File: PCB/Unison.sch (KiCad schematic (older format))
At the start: 223 parts, among them J1 USB4085-GF-A_REVA, U2 ATmega32U4-MU, Y1 16MHz

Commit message: Update pcb.
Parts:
- removed D72, D74, D76, D78, D80, D82, D85: D, SMK_ai03_RandomKeyboardParts:D_SOD-123-Pretty, symbol Device:D
- removed EXT1, EXT2: Conn_02x05_Odd_Even, Connector_PinHeader_1.27mm:PinHeader_2x05_P1.27mm_Horizontal, symbol Connector_Generic:Conn_02x05_Odd_Even
- removed ISO-Stab1: ISO-Stabilizer, MX_Alps_Hybrid:MXOnly-ISO-StabilizerOnly-Reversed, symbol Mechanical:MountingHole
- removed JP2, JP_AUDIO1: SolderJumper_2_Open, Jumper:SolderJumper-2_P1.3mm_Open_Pad1.0x1.5mm, symbol Jumper:SolderJumper_2_Open
- removed JP_LED3, JP_LED4: SolderJumper_3_Open, Jumper:SolderJumper-3_P1.3mm_Open_Pad1.0x1.5mm_NumberLabels, symbol Jumper:SolderJumper_3_Open
- removed LED1, LED2, LED3, LED4, LED5, LED6, LED7, LED8: SK6812MINI, LED_SMD:LED_SK6812MINI_PLCC4_3.5x3.5mm_P1.75mm_TriangleMark, symbol LED:SK6812MINI
- removed LED_PAD1: Conn_01x03, SMK_hsgw:LED_WS2812_tape_10mm, symbol Connector_Generic:Conn_01x03
- removed R8, R9: 4.7k, SMK_keebio:Resistor-Hybrid, symbol Device:R
- removed SW_'1, SW_:1, SW_@1, SW_CAPS1u1, SW_E1, SW_Fn1u1, SW_H1, SW_I1, SW_ISO1, SW_O1, SW_P1, SW_Q1, SW_R1, SW_RSFT1u1, SW_T1, SW_U1, SW_W1, SW_WIN1, SW_Y1, SW_[1, SW_[3, SW_]1, SW_]2: SW_Push, MX_Alps_Hybrid:MXOnly-1U-Hotswap, symbol Switch:SW_Push
- removed SW_10, SW_ESC2, SW_[2: SW_Push, MX_Alps_Hybrid:MXOnly-1U-NoLED, symbol Switch:SW_Push
- removed SW_BS1.5u1, SW_TAB1.5u1: SW_Push, MX_Alps_Hybrid:MXOnly-1.5U-Hotswap, symbol Switch:SW_Push
- removed SW_CMD1.25u1, SW_Fn1.25u1, SW_LOPT/LALT1.25u1, SW_ROPT/KANA1.25u1: SW_Push, MX_Alps_Hybrid:MXOnly-1.25U-Hotswap, symbol Switch:SW_Push
- removed SW_ENT1.25u1: SW_Push, MX_Alps_Hybrid:MXOnly-1.25U-NoLED, symbol Switch:SW_Push
- removed SW_ENT2.25u1: SW_Push, MX_Alps_Hybrid:MXOnly-2.25U-Hotswap-ReversedStabilizers, symbol Switch:SW_Push
- removed SW_LSFT1.75u1: SW_Push, MX_Alps_Hybrid:MXOnly-1.75U-Hotswap, symbol Switch:SW_Push
- removed SW_LSPC2u1, SW_RSPC2u1: SW_Push, MX_Alps_Hybrid:MXOnly-2U-Hotswap-ReversedStabilizers, symbol Switch:SW_Push
- removed SW_RSFT1.5u1: SW_Push, MX_Alps_Hybrid:MXOnly-1.5U-NoLED, symbol Switch:SW_Push
- added D10, D100, D11, D12, D30, D41, D53, D64, D65, D77, D8, D89, D90, D91, D92, D93, D94, D95, D96, D97, D98, D99: D, SMK_ai03_RandomKeyboardParts:D_SOD-123-Pretty, symbol Device:D
- added L1, L10, L11, L12, L13, L14, L2, L3, L4, L5, L6, L7, L8, L9: YS_SK6812MINI_E_modify_GND_powerInput, symbol mx2u:YS_SK6812MINI_E_modify_GND_powerInput
- added L15: SERIAL_LED_TAPE, symbol swanmatch:SERIAL_LED_TAPE
- added OL1: OLED, symbol swanmatch:OLED
- added SW_10_2, SW_12_1, SW_12_2, SW_13_2, SW_14, SW_17_1, SW_17_2, SW_18_2, SW_19_2, SW_20_2, SW_23_2, SW_24_2, SW_25_2, SW_25_3, SW_25_4, SW_27_1, SW_27_2, SW_28_2, SW_30, SW_32_1, SW_32_2, SW_35_2, SW_37_1, SW_37_2, SW_38_2, SW_39_2, SW_40_1, SW_40_2, SW_40_3, SW_40_4, SW_42, SW_45_2, SW_45_3, SW_45_4, SW_47, SW_52, SW_57, SW_6, SW_60_1, SW_60_2, SW_62, SW_67, SW_70_2, SW_70_3, SW_72, SW_75_2, SW_7_1, SW_7_2, SW_80_2, SW_82, SW_85_2, SW_85_3, SW_85_4, SW_87, SW_8_1, SW_8_2, SW_9, SW_90, SW_91_1, SW_94, SW_95, SW_97_1, SW_97_2, SW_98_2: SW_Push, ukiha:CherryMX_MidHeight_16mm_rev2, symbol Switch:SW_Push
- added SW_RE3, SW_RE4, SW_RE5, SW_RE6: Rotary_Encoder_Switch, Rotary_Encoder:RotaryEncoder_Alps_EC11E-Switch_Vertical_H20mm, symbol Device:Rotary_Encoder_Switch
- JP_LED1: Note (none) -> Use Front LEDs
- JP_LED2: Note (none) -> Use RE2 LED
- SW_10_1: renamed from SW_CAPS1.25u1; footprint MX_Alps_Hybrid:MXOnly-1.25U-NoLED -> ukiha:CherryMX_MidHeight_16mm_rev2
- SW_13_1: renamed from SW_CTL1.25u1; footprint MX_Alps_Hybrid:MXOnly-1.5U-Hotswap -> ukiha:CherryMX_MidHeight_16mm_rev2
- SW_15: renamed from SW_LongOPT1; footprint MX_Alps_Hybrid:MXOnly-1U-Hotswap -> ukiha:CherryMX_MidHeight_16mm_rev2
- SW_16: renamed from SW_ESC1; footprint MX_Alps_Hybrid:MXOnly-1U-Hotswap -> ukiha:CherryMX_MidHeight_16mm_rev2
- SW_18_1: renamed from SW_CTL1.5u1; footprint MX_Alps_Hybrid:MXOnly-1.25U-Hotswap -> ukiha:CherryMX_MidHeight_16mm_rev2
- SW_19_1: renamed from SW_LSFT2u1; footprint MX_Alps_Hybrid:MXOnly-2U-Hotswap-ReversedStabilizers -> ukiha:CherryMX_MidHeight_16mm_rev2
- SW_20_1: renamed from SW_LongCMD1.25u1; footprint MX_Alps_Hybrid:MXOnly-1.25U-Hotswap -> ukiha:CherryMX_MidHeight_16mm_rev2
- SW_21: renamed from SW_1; footprint MX_Alps_Hybrid:MXOnly-1U-Hotswap -> ukiha:CherryMX_MidHeight_16mm_rev2
- SW_23_1: renamed from SW_S1; footprint MX_Alps_Hybrid:MXOnly-1U-Hotswap -> ukiha:CherryMX_MidHeight_16mm_rev2
- SW_24_1: renamed from SW_X1; footprint MX_Alps_Hybrid:MXOnly-1U-Hotswap -> ukiha:CherryMX_MidHeight_16mm_rev2
- SW_25_1: renamed from SW_MHEN/CMD1u1; footprint MX_Alps_Hybrid:MXOnly-1U-Hotswap -> ukiha:CherryMX_MidHeight_16mm_rev2
- SW_26: renamed from SW_2; footprint MX_Alps_Hybrid:MXOnly-1U-Hotswap -> ukiha:CherryMX_MidHeight_16mm_rev2
- SW_28_1: renamed from SW_A1; footprint MX_Alps_Hybrid:MXOnly-1U-Hotswap -> ukiha:CherryMX_MidHeight_16mm_rev2
- SW_29: renamed from SW_Z1; footprint MX_Alps_Hybrid:MXOnly-1U-Hotswap -> ukiha:CherryMX_MidHeight_16mm_rev2
- SW_31: renamed from SW_3; footprint MX_Alps_Hybrid:MXOnly-1U-Hotswap -> ukiha:CherryMX_MidHeight_16mm_rev2
- SW_34: renamed from SW_V1; footprint MX_Alps_Hybrid:MXOnly-1U-Hotswap -> ukiha:CherryMX_MidHeight_16mm_rev2
- SW_35_1: renamed from SW_LSPC2.25u1; footprint MX_Alps_Hybrid:MXOnly-2.25U-Hotswap -> ukiha:CherryMX_MidHeight_16mm_rev2
- SW_36: renamed from SW_4; footprint MX_Alps_Hybrid:MXOnly-1U-Hotswap -> ukiha:CherryMX_MidHeight_16mm_rev2
- SW_38_1: renamed from SW_D1; footprint MX_Alps_Hybrid:MXOnly-1U-Hotswap -> ukiha:CherryMX_MidHeight_16mm_rev2
- SW_39_1: renamed from SW_C1; footprint MX_Alps_Hybrid:MXOnly-1U-Hotswap -> ukiha:CherryMX_MidHeight_16mm_rev2
- SW_41: renamed from SW_5; footprint MX_Alps_Hybrid:MXOnly-1U-Hotswap -> ukiha:CherryMX_MidHeight_16mm_rev2
- SW_43: renamed from SW_F1; footprint MX_Alps_Hybrid:MXOnly-1U-Hotswap -> ukiha:CherryMX_MidHeight_16mm_rev2
- SW_45_1: renamed from SW_RSPC6.25u1; footprint MX_Alps_Hybrid:MXOnly-6.25U-Hotswap-ReversedStabilizers -> ukiha:CherryMX_MidHeight_16mm_rev2
- SW_46: renamed from SW_6; footprint MX_Alps_Hybrid:MXOnly-1U-Hotswap -> ukiha:CherryMX_MidHeight_16mm_rev2
- SW_48: renamed from SW_G1; footprint MX_Alps_Hybrid:MXOnly-1U-Hotswap -> ukiha:CherryMX_MidHeight_16mm_rev2
- SW_49: renamed from SW_B1; footprint MX_Alps_Hybrid:MXOnly-1U-Hotswap -> ukiha:CherryMX_MidHeight_16mm_rev2
- SW_50: renamed from SW_RCMD/HEN1.25u1; footprint MX_Alps_Hybrid:MXOnly-1.25U-Hotswap -> ukiha:CherryMX_MidHeight_16mm_rev2
- SW_51: renamed from SW_7; footprint MX_Alps_Hybrid:MXOnly-1U-Hotswap -> ukiha:CherryMX_MidHeight_16mm_rev2
- SW_53: renamed from SW_H2; footprint MX_Alps_Hybrid:MXOnly-1U-NoLED -> ukiha:CherryMX_MidHeight_16mm_rev2
- SW_54: renamed from SW_N1; footprint MX_Alps_Hybrid:MXOnly-1U-Hotswap -> ukiha:CherryMX_MidHeight_16mm_rev2
- SW_56: renamed from SW_8; footprint MX_Alps_Hybrid:MXOnly-1U-Hotswap -> ukiha:CherryMX_MidHeight_16mm_rev2
- SW_58: renamed from SW_J1; footprint MX_Alps_Hybrid:MXOnly-1U-Hotswap -> ukiha:CherryMX_MidHeight_16mm_rev2
- SW_59: renamed from SW_M1; footprint MX_Alps_Hybrid:MXOnly-1U-Hotswap -> ukiha:CherryMX_MidHeight_16mm_rev2
- SW_61: renamed from SW_9; footprint MX_Alps_Hybrid:MXOnly-1U-Hotswap -> ukiha:CherryMX_MidHeight_16mm_rev2
- SW_63: renamed from SW_K1; footprint MX_Alps_Hybrid:MXOnly-1U-Hotswap -> ukiha:CherryMX_MidHeight_16mm_rev2
- SW_64: renamed from SW_<1; footprint MX_Alps_Hybrid:MXOnly-1U-Hotswap -> ukiha:CherryMX_MidHeight_16mm_rev2
- SW_65: renamed from SW_ROPT/KANA1.25u2; footprint MX_Alps_Hybrid:MXOnly-1.25U-Hotswap -> ukiha:CherryMX_MidHeight_16mm_rev2
- SW_68: renamed from SW_L1; footprint MX_Alps_Hybrid:MXOnly-1U-Hotswap -> ukiha:CherryMX_MidHeight_16mm_rev2
- SW_69: renamed from SW_>1; footprint MX_Alps_Hybrid:MXOnly-1U-Hotswap -> ukiha:CherryMX_MidHeight_16mm_rev2
- SW_70_1: renamed from SW_LEFT1; footprint MX_Alps_Hybrid:MXOnly-1U-Hotswap -> ukiha:CherryMX_MidHeight_16mm_rev2
- SW_71: renamed from SW_-1; footprint MX_Alps_Hybrid:MXOnly-1U-Hotswap -> ukiha:CherryMX_MidHeight_16mm_rev2
- SW_73: renamed from SW_;1; footprint MX_Alps_Hybrid:MXOnly-1U-Hotswap -> ukiha:CherryMX_MidHeight_16mm_rev2
- SW_74: renamed from SW_/1; footprint MX_Alps_Hybrid:MXOnly-1U-Hotswap -> ukiha:CherryMX_MidHeight_16mm_rev2
- SW_75_1: renamed from SW_MENU/ROPT1; footprint MX_Alps_Hybrid:MXOnly-1U-Hotswap -> ukiha:CherryMX_MidHeight_16mm_rev2
- SW_76: renamed from SW_0; footprint MX_Alps_Hybrid:MXOnly-1U-Hotswap -> ukiha:CherryMX_MidHeight_16mm_rev2
- SW_78: renamed from SW_ENT1.5u1; footprint MX_Alps_Hybrid:MXOnly-1.5U-NoLED -> ukiha:CherryMX_MidHeight_16mm_rev2
- SW_79: renamed from SW_RSFT1.75u1; footprint MX_Alps_Hybrid:MXOnly-1.75U-Hotswap -> ukiha:CherryMX_MidHeight_16mm_rev2
- SW_80_1: renamed from SW_RIGHT1; footprint MX_Alps_Hybrid:MXOnly-1U-Hotswap -> ukiha:CherryMX_MidHeight_16mm_rev2
- SW_81: renamed from SW_\1; footprint MX_Alps_Hybrid:MXOnly-1U-Hotswap -> ukiha:CherryMX_MidHeight_16mm_rev2
- SW_83: renamed from SW_'2; footprint MX_Alps_Hybrid:MXOnly-1U-NoLED -> ukiha:CherryMX_MidHeight_16mm_rev2
- SW_84: renamed from SW_up1; footprint MX_Alps_Hybrid:MXOnly-1U-Hotswap -> ukiha:CherryMX_MidHeight_16mm_rev2
- SW_85_1: renamed from SW_DOWN1; footprint MX_Alps_Hybrid:MXOnly-1U-Hotswap -> ukiha:CherryMX_MidHeight_16mm_rev2
- SW_86: renamed from SW_=1; footprint MX_Alps_Hybrid:MXOnly-1U-Hotswap -> ukiha:CherryMX_MidHeight_16mm_rev2
- SW_89: renamed from SW_Fn1.5u1; footprint MX_Alps_Hybrid:MXOnly-1.5U-NoLED -> ukiha:CherryMX_MidHeight_16mm_rev2
- SW_96: renamed from SW_`1; footprint MX_Alps_Hybrid:MXOnly-1U-Hotswap -> ukiha:CherryMX_MidHeight_16mm_rev2
- SW_98_1: renamed from SW_FN1.75u1; footprint MX_Alps_Hybrid:MXOnly-1.75U-NoLED -> ukiha:CherryMX_MidHeight_16mm_rev2
- renumbered D66 to D1, D71 to D102, D67 to D13, D73 to D14, D11 to D15, D7 to D16, D8 to D17, D9 to D18, D10 to D19, D86 to D2, D16 to D20, D12 to D21, D13 to D22, D14 to D23, D15 to D24, D75 to D25, D21 to D26, D17 to D27, D18 to D28, D19 to D29, D1 to D3, D25 to D31, D22 to D32, D23 to D33, D24 to D34, D20 to D35, D77 to D36, D29 to D37, D26 to D38, D27 to D39, D2 to D4, D28 to D40, D33 to D42, D38 to D43, D39 to D44, D40 to D45, D68 to D46, D79 to D47, D37 to D48, D42 to D49, D3 to D5, D43 to D50, D44 to D51, D69 to D52, D41 to D54, D47 to D55, D48 to D56, D49 to D57, D45 to D58, D81 to D59, D4 to D6, D46 to D60, D30 to D61, D31 to D62, D32 to D63, D51 to D66, D34 to D67, D35 to D68, D36 to D69, D5 to D7, D50 to D70, D84 to D71, D56 to D72, D52 to D73, D53 to D74, D54 to D75, D55 to D76, D61 to D78, D57 to D79, D58 to D80, D59 to D81, D60 to D82, D62 to D84, D63 to D85, D64 to D86, D70 to D87, D65 to D88, D6 to D9, R7 to R1, R5 to R4, R1 to R5, R2 to R6, R4 to R7, R3 to R8, R6 to R9, U2 to U1
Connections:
- net labels added: AUDIO1, AUDIO2[Reserve], RE3_1, RE3_2, RE3_A, RE3_B, RE4_1, RE4_2, RE4_A, RE4_B, RE5_1, RE5_2, RE5_A, RE5_B, RE6_1, RE6_2, RE6_A, RE6_B, SCL_RE2B, SDA_RE2A
- net labels removed: AUDIO, RE2_A, RE2_B, Reserve_PB4, Reserve_PB5, Reserve_PB6, Reserve_PC6, Reserve_PD2-RX, Reserve_PD3-TX, SCL, SDA, pin11
- wire segments 323 -> 585
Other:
- note added: "Audio pins\nGroup1: B5, B6, B7\nGroup2: C4, C5, C6"
- note added: "Layer Indicator"
- note added: "Optional: OLED alternate"
- note added: "Rotary Encoder Indicator (2nd R.E. is OLED alternate)"
- note added: "SW_01"
- note added: "SW_02"
- note added: "SW_03"
- note added: "SW_04"
- note added: "SW_05"
- note added: "SW_92"
- note added: "SW_93\nReserved"
- note added: "Volume Indicator"
- note removed: "Use Left LEDs"
- note removed: "Use Right LEDs"
- moved on the sheet: C1, C2, C3, C4, C5, C6, C7, D1, D102, D13, D14, D15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

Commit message: Update v01完成
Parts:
- removed L15: SERIAL_LED_TAPE, symbol swanmatch:SERIAL_LED_TAPE
- added J2: Conn_02x01, Connector_PinHeader_2.54mm:PinHeader_2x01_P2.54mm_Vertical, symbol Connector_Generic:Conn_02x01
- added L15: SERIAL_LED_TAPE, ukiha:StripLED_rev3, symbol local_library:SERIAL_LED_TAPE
- added SW_23_3, SW_32_3: SW_Push, ukiha:CherryMX_MidHeight_16mm_rev2, symbol Switch:SW_Push
- C1, C2, C3, C4, C5, C6, C7: footprint Capacitor_SMD:C_0805_2012Metric_Pad1.15x1.40mm_HandSolder -> Capacitor_SMD:C_0805_2012Metric_Pad1.18x1.45mm_HandSolder
- D1, D10, D100, D11, D12, D13, D14, D15, D16, D17, D18, D19, D2, D20, D21, D22, D23, D24, D25, D26, D27, D28, D29, D3, D30, D31, D32, D33, D34, D35, D36, D37, D38, D39, D4, D40, D41, D42, D43, D44, D45, D46, D47, D48, D49, D5, D50, D51, D52, D53, D54, D55, D56, D57, D58, D59, D6, D60, D61, D62, D63, D64, D65, D66, D67, D68, D69, D7, D70, D71, D72, D73, D74, D75, D76, D77, D78, D79, D8, D80, D81, D82, D83, D84, D85, D86, D87, D88, D89, D9, D90, D91, D92, D93, D94, D95, D96, D97, D98, D99: footprint SMK_ai03_RandomKeyboardParts:D_SOD-123-Pretty -> Diode_SMD:D_SOD-123
- J1: footprint Connector_USB:USB_C_Receptacle_GCT_USB4085_pad_modified -> USB4085:GCT_USB4085-GF-A_REVA
- L1, L10, L11, L12, L13, L14, L2, L3, L4, L5, L6, L7, L8, L9: footprint (none) -> mx2u:YS-SK6812MINI-E
- OL1: footprint (none) -> ukiha:OLED_rev2
- R1, R4, R5, R6, R7, R8, R9: footprint Resistor_SMD:R_0805_2012Metric_Pad1.15x1.40mm_HandSolder -> Resistor_SMD:R_0805_2012Metric_Pad1.20x1.40mm_HandSolder
- ResetSW1: footprint SMK_ai03_RandomKeyboardParts:SKQG-1155865 -> Button_Switch_SMD:SW_SPST_SKQG_WithStem
- SW_10_2, SW_19_2, SW_24_2, SW_39_2, SW_45_4: footprint ukiha:CherryMX_MidHeight_16mm_rev2 -> ukiha:CherryMX_MidHeight_16mm_rev2_2u_guide
- SW_17_2, SW_18_2, SW_23_2, SW_25_3, SW_32_2, SW_37_2, SW_38_2, SW_40_2, SW_45_2, SW_70_2, SW_75_2, SW_7_2, SW_85_3, SW_8_2, SW_97_2, SW_98_2: footprint ukiha:CherryMX_MidHeight_16mm_rev2 -> ukiha:CherryMX_MidHeight_16mm_rev2_1.5u_guide
- SW_20_2, SW_25_4, SW_35_2, SW_40_3, SW_40_4, SW_45_3, SW_70_3, SW_80_2, SW_85_2, SW_85_4: footprint ukiha:CherryMX_MidHeight_16mm_rev2 -> ukiha:CherryMX_MidHeight_16mm_rev2_1.25u_guide
- SW_25_2, SW_60_2: footprint ukiha:CherryMX_MidHeight_16mm_rev2 -> ukiha:CherryMX_MidHeight_16mm_rev2_2U_vertical_guide
- U1: footprint SMK_keebio:QFN-44-1EP_7x7mm_Pitch0.5mm -> swanmatch:QFN-44-1EP_7x7mm_Pitch0.5mm
- renumbered SW_91_1 to SW_91
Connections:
- wire segments 585 -> 587
- no-connect marks 4 -> 6
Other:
- note added: "1 2 3 4 5 6 7 8 9 10 11 12 13 14 15 16 17\n17 16 15 14 13 12 11 10 9 8 7 6 5 4 3 2 1"
- note added: "1 2 3 4 5 6 7 8 9/0"
- note added: "SW_93\nReserve"
- note removed: "SW_93\nReserved"
- moved on the sheet: D8, JP_LED1, JP_LED2, L1, L10, L11, L12, L13, L14, L2, L3, L4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

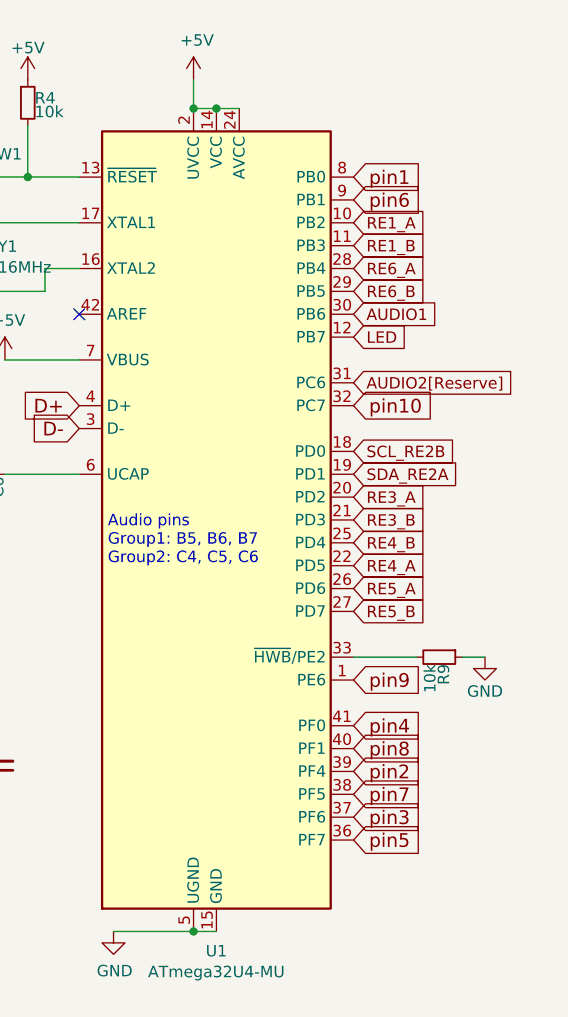
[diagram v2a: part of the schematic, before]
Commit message: Update: Change MCU from ATMega32u4-MU  to ATMega32u4-AU.
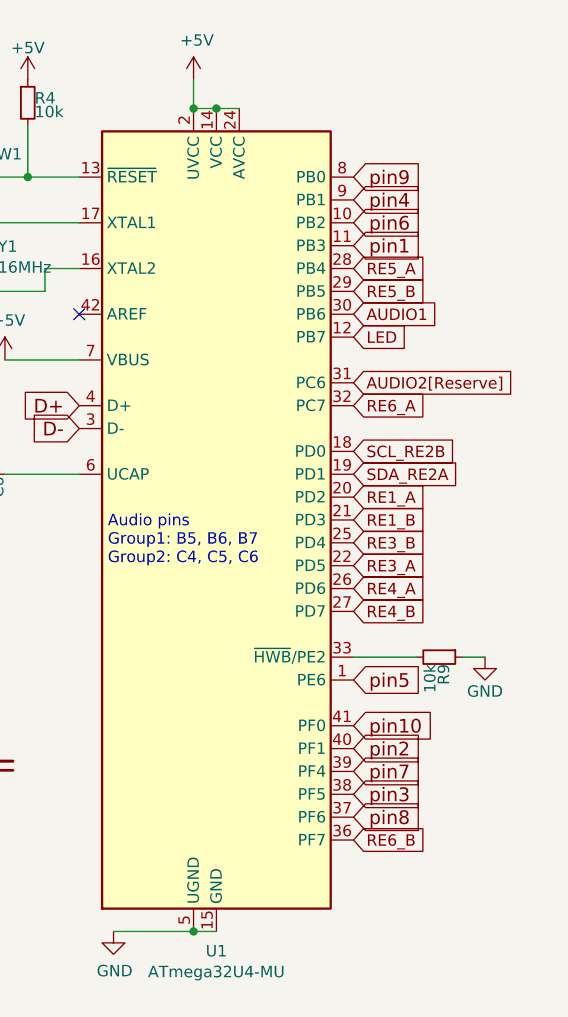
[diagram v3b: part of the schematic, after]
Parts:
- U1: footprint swanmatch:QFN-44-1EP_7x7mm_Pitch0.5mm -> keebio:ATMEGA32U4-AU
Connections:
- net RE1_A: now also U1.20 (PD2); no longer U1.10 (PB2)
- net RE1_B: now also U1.21 (PD3); no longer U1.11 (PB3)
- net RE3_A: now also U1.22 (PD5); no longer U1.20 (PD2)
- net RE3_B: now also U1.25 (PD4); no longer U1.21 (PD3)
- net RE4_A: now also U1.26 (PD6); no longer U1.22 (PD5)
- net RE4_B: now also U1.27 (PD7); no longer U1.25 (PD4)
- net RE5_A: now also U1.28 (PB4); no longer U1.26 (PD6)
- net RE5_B: now also U1.29 (PB5); no longer U1.27 (PD7)
- net RE6_A: now also U1.32 (PC7); no longer U1.28 (PB4)
- net RE6_B: now also U1.36 (PF7); no longer U1.29 (PB5)
- net pin1: now also U1.11 (PB3); no longer U1.8 (PB0)
- net pin10: now also U1.41 (PF0); no longer U1.32 (PC7)
- net pin2: now also U1.40 (PF1); no longer U1.39 (PF4)
- net pin3: now also U1.38 (PF5); no longer U1.37 (PF6)
- net pin4: now also U1.9 (PB1); no longer U1.41 (PF0)
- net pin5: now also U1.1 (PE6); no longer U1.36 (PF7)
- net pin6: now also U1.10 (PB2); no longer U1.9 (PB1)
- net pin7: now also U1.39 (PF4); no longer U1.38 (PF5)
- net pin8: now also U1.37 (PF6); no longer U1.40 (PF1)
- net pin9: now also U1.8 (PB0); no longer U1.1 (PE6)
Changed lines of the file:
@@
 	-1   0    0    1
 $EndComp
-Text GLabel 15300 2225 2    60   Input ~ 0
+Text GLabel 15300 2325 2    60   Input ~ 0
 pin6
-Text GLabel 15300 5025 2    60   Input ~ 0
+Text GLabel 15300 4325 2    60   Input ~ 0
 pin5
-Text GLabel 15300 4525 2    60   Input ~ 0
+Text GLabel 15300 2225 2    60   Input ~ 0
 pin4
-Text GLabel 15300 4925 2    60   Input ~ 0
+Text GLabel 15300 4825 2    60   Input ~ 0
 pin3
-Text GLabel 15300 4725 2    60   Input ~ 0
+Text GLabel 15300 4625 2    60   Input ~ 0
 pin2
-Text GLabel 15300 2125 2    60   Input ~ 0
+Text GLabel 15300 2425 2    60   Input ~ 0
 pin1
-Text GLabel 15300 3125 2    60   Input ~ 0
+Text GLabel 15300 4525 2    60   Input ~ 0
 pin10
 Wire Wire Line
@@
 F 0 "U1" H 14700 1739 50  0000 C CNN
 F 1 "ATmega32U4-MU" H 14700 1648 50  0000 C CNN
-F 2 "swanmatch:QFN-44-1EP_7x7mm_Pitch0.5mm" H 14700 3625 50  0001 C CIN
+F 2 "keebio:ATMEGA32U4-AU" H 14700 3625 50  0001 C CIN
 F 3 "http://ww1.microchip.com/downloads/en/DeviceDoc/Atmel-7766-8-bit-AVR-ATmega16U4-32U4_Datasheet.pdf" H 14700 3625 50  0001 C CNN
 F 4 "C45874" H 14700 3625 50  0001 C CNN "LCSC"
@@
 	1    0    0    -1
 $EndComp
-Text GLabel 15300 2325 2    50   Input ~ 0
+Text GLabel 15300 3525 2    50   Input ~ 0
 RE1_A
-Text GLabel 15300 2425 2    50   Input ~ 0
+Text GLabel 15300 3625 2    50   Input ~ 0
 RE1_B
 $Comp
@@
 Wire Wire Line
 	925  10025 925  10225
-Text GLabel 15300 2525 2    50   Input ~ 0
+Text GLabel 15300 3125 2    50   Input ~ 0
 RE6_A
 Text GLabel 15300 2725 2    50   Input ~ 0
@@
 Text GLabel 15300 2825 2    50   Input ~ 0
 LED
-Text GLabel 15300 2625 2    50   Input ~ 0
+Text GLabel 15300 5025 2    50   Input ~ 0
 RE6_B
-Text GLabel 15300 4325 2    60   Input ~ 0
+Text GLabel 15300 2125 2    60   Input ~ 0
 pin9
-Text GLabel 15300 4625 2    60   Input ~ 0
+Text GLabel 15300 4925 2    60   Input ~ 0
 pin8
-Text GLabel 15300 4825 2    60   Input ~ 0
+Text GLabel 15300 4725 2    60   Input ~ 0
 pin7
 $Comp
@@
 Text Notes 14225 3825 0    50   ~ 0
 Audio pins\nGroup1: B5, B6, B7\nGroup2: C4, C5, C6
-Text GLabel 15300 3525 2    50   Input ~ 0
+Text GLabel 15300 3825 2    50   Input ~ 0
 RE3_A
-Text GLabel 15300 3625 2    50   Input ~ 0
+Text GLabel 15300 3725 2    50   Input ~ 0
 RE3_B
-Text GLabel 15300 3825 2    50   Input ~ 0
+Text GLabel 15300 3925 2    50   Input ~ 0
 RE4_A
-Text GLabel 15300 3725 2    50   Input ~ 0
+Text GLabel 15300 4025 2    50   Input ~ 0
 RE4_B
-Text GLabel 15300 3925 2    50   Input ~ 0
+Text GLabel 15300 2525 2    50   Input ~ 0
 RE5_A
-Text GLabel 15300 4025 2    50   Input ~ 0
+Text GLabel 15300 2625 2    50   Input ~ 0
 RE5_B
 Text GLabel 4450 11000 2    50   Input ~ 0

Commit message: Update: MCUをMUからAUに変更し、配線をやり直した。
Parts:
- SW_37_2: footprint ukiha:CherryMX_MidHeight_16mm_rev2_1.5u_guide -> ukiha:CherryMX_MidHeight_16mm_rev2_1.5u_alt_guide
- U1: value ATmega32U4-MU -> ATmega32U4-AU; symbol MCU_Microchip_ATmega:ATmega32U4-MU -> MCU_Microchip_ATmega:ATmega32U4-AU
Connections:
- net GND: no longer U1.45 (GND)
- net RE1_A: now also U1.8 (PB0); no longer U1.20 (PD2)
- net RE1_B: now also U1.9 (PB1); no longer U1.21 (PD3)
- net RE3_A: now also U1.21 (PD3); no longer U1.22 (PD5)
- net RE3_B: now also U1.20 (PD2); no longer U1.25 (PD4)
- net RE4_A: now also U1.22 (PD5); no longer U1.26 (PD6)
- net RE4_B: now also U1.25 (PD4); no longer U1.27 (PD7)
- net RE5_A: now also U1.26 (PD6); no longer U1.28 (PB4)
- net RE5_B: now also U1.27 (PD7); no longer U1.29 (PB5)
- net RE6_A: now also U1.28 (PB4); no longer U1.32 (PC7)
- net RE6_B: now also U1.29 (PB5); no longer U1.36 (PF7)
- net pin10: now also U1.32 (PC7); no longer U1.41 (PF0)
- net pin2: now also U1.1 (PE6); no longer U1.40 (PF1)
- net pin3: now also U1.40 (PF1); no longer U1.38 (PF5)
- net pin4: now also U1.38 (PF5); no longer U1.9 (PB1)
- net pin5: now also U1.36 (PF7); no longer U1.1 (PE6)
- net pin7: now also U1.41 (PF0); no longer U1.39 (PF4)
- net pin8: now also U1.39 (PF4); no longer U1.37 (PF6)
- net pin9: now also U1.37 (PF6); no longer U1.8 (PB0)
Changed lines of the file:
@@
 Text GLabel 15300 2325 2    60   Input ~ 0
 pin6
-Text GLabel 15300 4325 2    60   Input ~ 0
+Text GLabel 15300 5025 2    60   Input ~ 0
 pin5
-Text GLabel 15300 2225 2    60   Input ~ 0
-pin4
 Text GLabel 15300 4825 2    60   Input ~ 0
-pin3
+pin4
 Text GLabel 15300 4625 2    60   Input ~ 0
+pin3
+Text GLabel 15300 4325 2    60   Input ~ 0
 pin2
 Text GLabel 15300 2425 2    60   Input ~ 0
 pin1
-Text GLabel 15300 4525 2    60   Input ~ 0
+Text GLabel 15300 3125 2    60   Input ~ 0
 pin10
 Wire Wire Line
@@
 	13250 4900 13500 4900
 $Comp
-L MCU_Microchip_ATmega:ATmega32U4-MU U1
+L MCU_Microchip_ATmega:ATmega32U4-AU U1
 U 1 1 5D93C3AA
 P 14700 3625
 F 0 "U1" H 14700 1739 50  0000 C CNN
-F 1 "ATmega32U4-MU" H 14700 1648 50  0000 C CNN
+F 1 "ATmega32U4-AU" H 14700 1648 50  0000 C CNN
 F 2 "keebio:ATMEGA32U4-AU" H 14700 3625 50  0001 C CIN
 F 3 "http://ww1.microchip.com/downloads/en/DeviceDoc/Atmel-7766-8-bit-AVR-ATmega16U4-32U4_Datasheet.pdf" H 14700 3625 50  0001 C CNN
@@
 	1    0    0    -1
 $EndComp
-Text GLabel 15300 3525 2    50   Input ~ 0
+Text GLabel 15300 2125 2    50   Input ~ 0
 RE1_A
-Text GLabel 15300 3625 2    50   Input ~ 0
+Text GLabel 15300 2225 2    50   Input ~ 0
 RE1_B
 $Comp
@@
 Wire Wire Line
 	925  10025 925  10225
-Text GLabel 15300 3125 2    50   Input ~ 0
+Text GLabel 15300 2525 2    50   Input ~ 0
 RE6_A
 Text GLabel 15300 2725 2    50   Input ~ 0
@@
 Text GLabel 15300 2825 2    50   Input ~ 0
 LED
-Text GLabel 15300 5025 2    50   Input ~ 0
+Text GLabel 15300 2625 2    50   Input ~ 0
 RE6_B
-Text GLabel 15300 2125 2    60   Input ~ 0
-pin9
 Text GLabel 15300 4925 2    60   Input ~ 0
-pin8
+pin9
 Text GLabel 15300 4725 2    60   Input ~ 0
+pin8
+Text GLabel 15300 4525 2    60   Input ~ 0
 pin7
 $Comp
@@
 Text Notes 14225 3825 0    50   ~ 0
 Audio pins\nGroup1: B5, B6, B7\nGroup2: C4, C5, C6
-Text GLabel 15300 3825 2    50   Input ~ 0
+Text GLabel 15300 3625 2    50   Input ~ 0
 RE3_A
-Text GLabel 15300 3725 2    50   Input ~ 0
+Text GLabel 15300 3525 2    50   Input ~ 0
 RE3_B
-Text GLabel 15300 3925 2    50   Input ~ 0
+Text GLabel 15300 3825 2    50   Input ~ 0
 RE4_A
-Text GLabel 15300 4025 2    50   Input ~ 0
+Text GLabel 15300 3725 2    50   Input ~ 0
 RE4_B
-Text GLabel 15300 2525 2    50   Input ~ 0
+Text GLabel 15300 3925 2    50   Input ~ 0
 RE5_A
-Text GLabel 15300 2625 2    50   Input ~ 0
+Text GLabel 15300 4025 2    50   Input ~ 0
 RE5_B
 Text GLabel 4450 11000 2    50   Input ~ 0
@@
 F 0 "SW_37_2" H 3700 4160 50  0000 C CNN
 F 1 "SW_Push" H 3700 4069 50  0000 C CNN
-F 2 "ukiha:CherryMX_MidHeight_16mm_rev2_1.5u_guide" H 3700 4075 50  0001 C CNN
+F 2 "ukiha:CherryMX_MidHeight_16mm_rev2_1.5u_alt_guide" H 3700 4075 50  0001 C CNN
 F 3 "~" H 3700 4075 50  0001 C CNN
 	1    3700 3875
